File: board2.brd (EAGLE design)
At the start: 100 x 80 mm, 76 parts, among them Q1 7.68M, Q2 16MHz

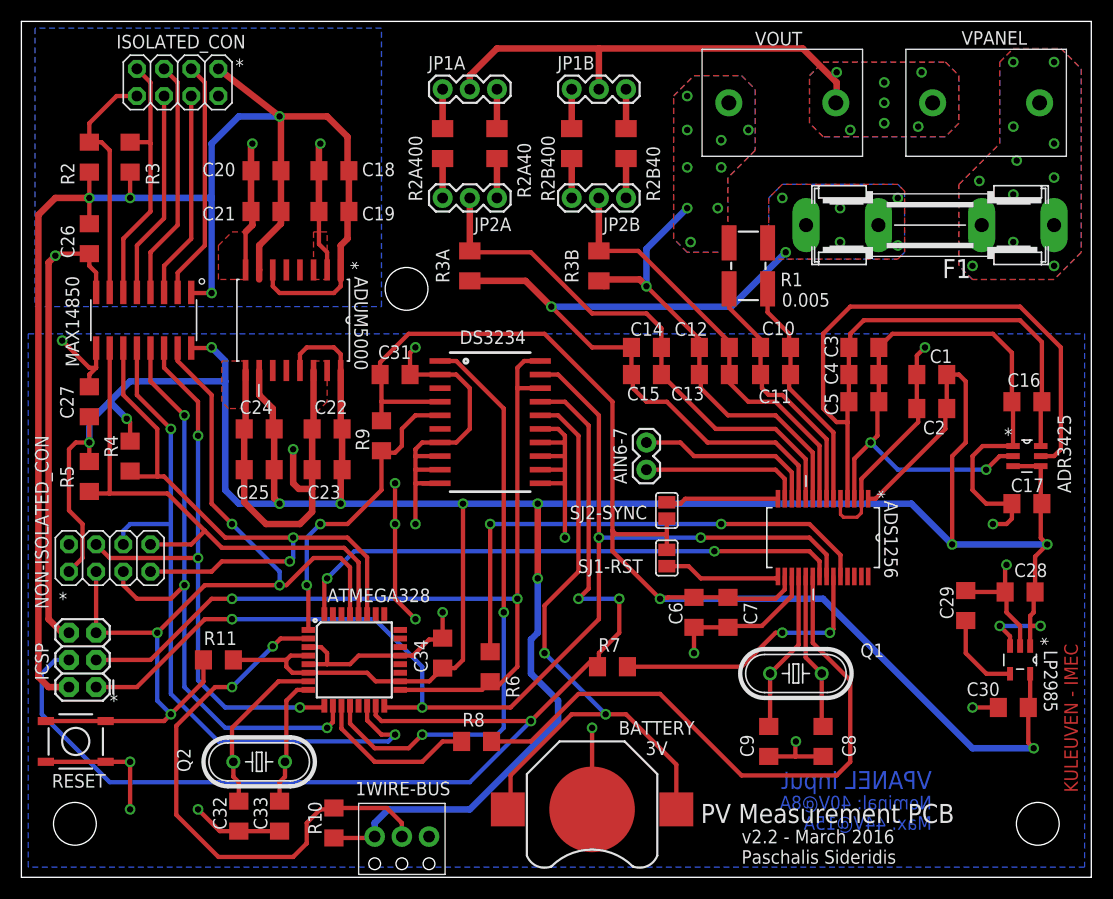
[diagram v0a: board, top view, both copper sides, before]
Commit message: Added RX-TX pin jumpers. IMPORTANT: changed the 5V&GND of ICSP connector to the isolated side (after iso)
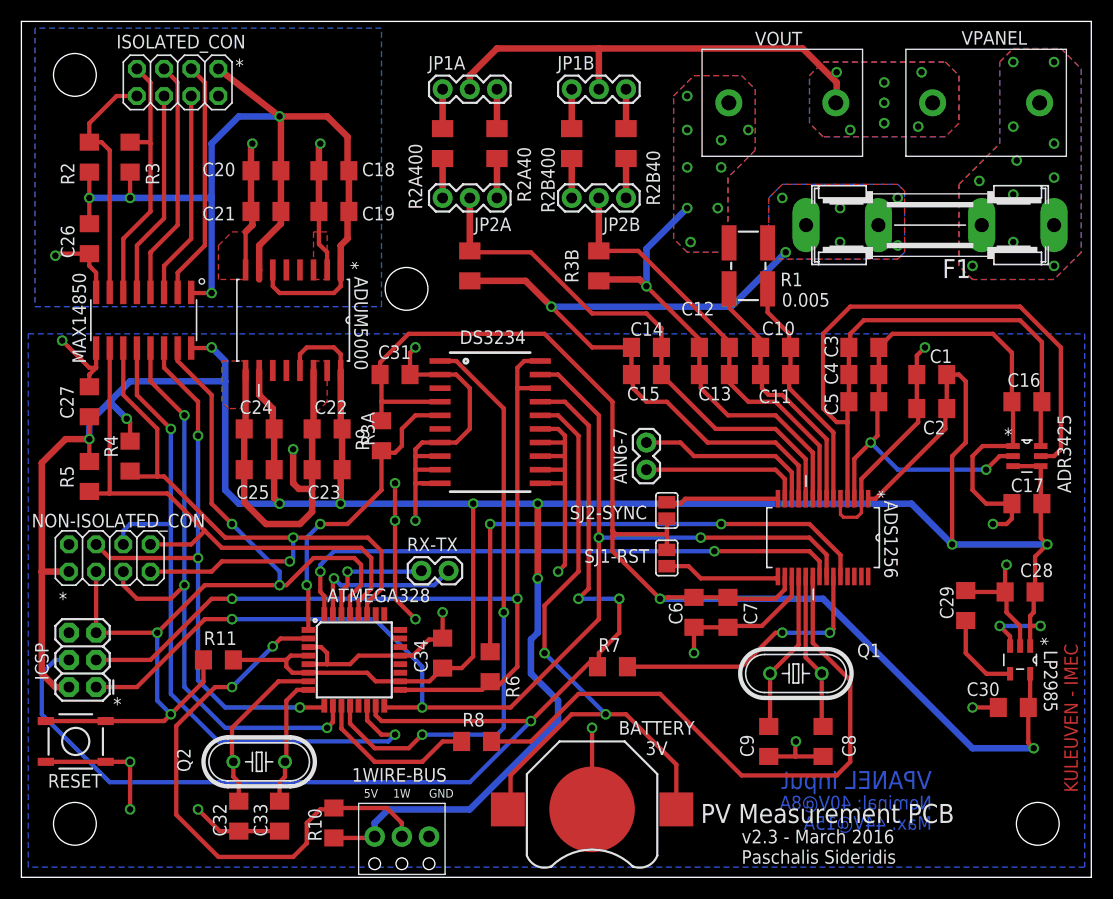
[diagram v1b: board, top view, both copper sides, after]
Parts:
- added RX-TX: (no value), SparkFun-Connectors:1X02
- Q1: value 7.68M -> 7.68MHz
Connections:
- new net RX: ATMEGA328.30, RX-TX.1
- new net TX: ATMEGA328.31, RX-TX.2
- net 5V: no longer ICSP.2
- net 5V_ISO: now also ICSP.2
- net GND: no longer ICSP.6
- net GND_ISO: now also ICSP.6
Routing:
- net 5V: track 148.3 -> 96.5 mm
- net GND: track 68.2 -> 31.5 mm
- net 5V_ISO: track 317.3 -> 333.7 mm
- net TX: track 0.00 -> 14.9 mm, vias 0 -> 1
- net RX: track 0.00 -> 11.1 mm, vias 0 -> 1
- net GND_ISO: track 272.6 -> 275.7 mm
- net SDA_ISO: track 59.9 -> 62.1 mm
- net SCL_ISO: track 53.0 -> 54.9 mm
- net RESET: track 89.6 -> 91.2 mm
- net ADC_DRDY: track 52.3 -> 53.8 mm
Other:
- board text added: "1W"
- board text added: "5V"
- board text added: "GND"
- board text added: "v2.3 - March 2016 Paschalis Sideridis"
- board text removed: "v2.2 - March 2016 Paschalis Sideridis"
